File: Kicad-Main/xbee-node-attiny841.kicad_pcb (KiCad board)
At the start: 2 copper layers, 58.5 x 58.5 mm, 41 parts, among them P10 CONN_1, P11 CONN_1, P12 CONN_1, P13 CONN_1, P14 CONN_1, P15 CONN_1, P16 CONN_1, P17 CONN_1, P18 CONN_1, P2 XBee Adaptor, P3 Test, P4 Battery, P5 XBee-ext-1, P6 XBee-ext-2, P7 CONN_1, P8 CONN_1, P9 CONN_1, Q2 S9014, Q3 2N7000, U1 ATTINY84-S, U2 MAX952ESA, U3 TPS77033

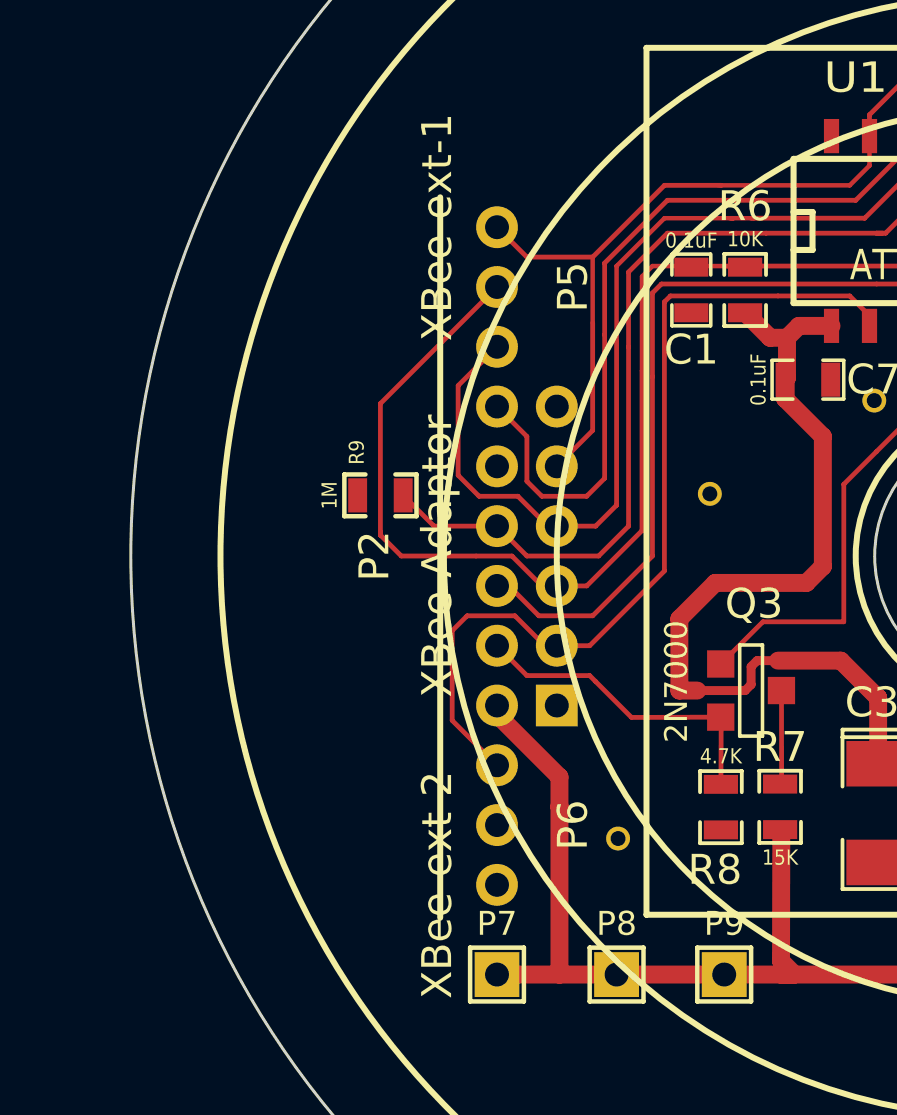
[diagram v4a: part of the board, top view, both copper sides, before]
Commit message: Create version 4 of the XBee mount board and modify the main board to allow the XBee base to sit on the main board.
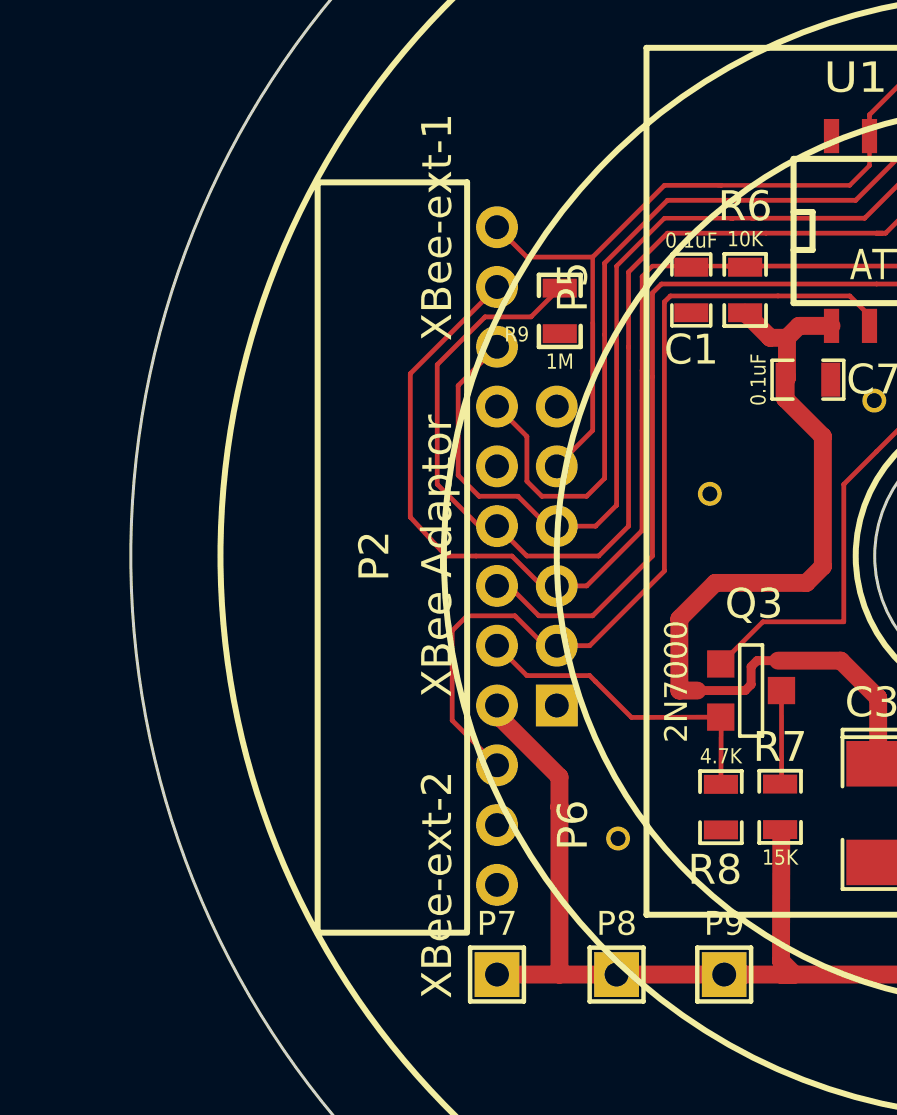
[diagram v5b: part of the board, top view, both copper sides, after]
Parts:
- moved R9 8.61 mm to (185.1, 91.8), turned to 90 degrees
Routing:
- net /Sleep-Rq: track 31.4 -> 39.5 mm
- net /Reset: track 73.8 -> 72.0 mm
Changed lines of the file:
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@@
     (area 162.31 68.7 242.200001 132.330001)
     (thickness 1.6)
-    (drawings 11)
-    (tracks 331)
+    (drawings 14)
+    (tracks 334)
     (zones 0)
     (modules 41)
@@
   )
   (layers
-    (0 F.Cu signal hide)
-    (31 B.Cu power)
+    (0 F.Cu signal)
+    (31 B.Cu power hide)
     (32 B.Adhes user hide)
     (33 F.Adhes user hide)
@@
   )
   (setup
-    (last_trace_width 0.6)
+    (last_trace_width 0.16)
     (user_trace_width 0.3)
     (user_trace_width 0.6)
@@
   )
   (module SMD_Packages:SMD-0603_r (layer F.Cu)
-    (at 179.1 97.97)
-    (attr smd)
-    (fp_text reference R9 (at -0.79 -1.44 90) (layer F.SilkS)
+    (at 185.1 91.8 90)
+    (attr smd)
+    (fp_text reference R9 (at -0.79 -1.44 180) (layer F.SilkS)
       (effects (font (size 0.50038 0.4572) (thickness 0.1143)))
     )
-    (fp_text value 1M (at -1.69926 0 90) (layer F.SilkS)
+    (fp_text value 1M (at -1.69926 0 180) (layer F.SilkS)
       (effects (font (size 0.508 0.4572) (thickness 0.1143)))
     )
@@
     (fp_line (start 1.2065 -0.6985) (end 1.2065 0.6985) (layer F.SilkS) (width 0.15))
     (fp_line (start 1.2065 0.6985) (end 0.50038 0.6985) (layer F.SilkS) (width 0.15))
-    (pad 1 smd rect (at -0.762 0) (size 0.635 1.143) (layers F.Cu F.Paste F.Mask)
-      (net 9 GND))
-    (pad 2 smd rect (at 0.762 0) (size 0.635 1.143) (layers F.Cu F.Paste F.Mask)
+    (pad 1 smd rect (at -0.762 0 90) (size 0.635 1.143) (layers F.Cu F.Paste F.Mask)
+      (net 9 GND))
+    (pad 2 smd rect (at 0.762 0 90) (size 0.635 1.143) (layers F.Cu F.Paste F.Mask)
       (net 5 /Sleep-Rq))
     (model smd\resistors\R0603.wrl
@@
     )
   )
+  (gr_line (start 182 112.6) (end 177 112.6) (angle 90) (layer F.SilkS) (width 0.2))
+  (gr_line (start 182 87.5) (end 177 87.5) (angle 90) (layer F.SilkS) (width 0.2))
+  (gr_line (start 177 112.5) (end 177 87.5) (angle 90) (layer F.SilkS) (width 0.2))
   (gr_circle (center 200 100) (end 215 99.9) (layer F.SilkS) (width 0.2))
   (gr_circle (center 200 100) (end 226.25 100) (layer F.SilkS) (width 0.2))
@@
   (gr_circle (center 200 100) (end 205 100) (layer F.SilkS) (width 0.2))
   (gr_circle (center 200 100) (end 218.75 99) (layer F.SilkS) (width 0.2))
-  (gr_line (start 181.1 112.1) (end 181.1 88) (angle 90) (layer F.SilkS) (width 0.2))
+  (gr_line (start 182 112.5) (end 182 87.5) (angle 90) (layer F.SilkS) (width 0.2))
   (gr_line (start 188 83) (end 188 112) (angle 90) (layer F.SilkS) (width 0.2))
   (gr_line (start 212 83) (end 188 83) (angle 90) (layer F.SilkS) (width 0.2))
@@
   (segment (start 188.6 87.6) (end 186.2 90) (width 0.16) (layer F.Cu) (net 2))
   (segment (start 190.5 87.6) (end 188.6 87.6) (width 0.16) (layer F.Cu) (net 2))
-  (segment (start 182.3 100) (end 179.8 100) (width 0.16) (layer F.Cu) (net 3))
+  (segment (start 182.3 100) (end 181.3 100) (width 0.16) (layer F.Cu) (net 3))
   (segment (start 183.5 100) (end 182.3 100) (width 0.16) (layer F.Cu) (net 3))
   (segment (start 184.5 101) (end 183.5 100) (width 0.16) (layer F.Cu) (net 3))
-  (segment (start 179.8 100) (end 179.1 99.3) (width 0.16) (layer F.Cu) (net 3))
+  (segment (start 181.3 100) (end 180.1 98.7) (width 0.16) (layer F.Cu) (net 3))
   (segment (start 185 101) (end 184.5 101) (width 0.16) (layer F.Cu) (net 3))
-  (segment (start 179.1 94.9) (end 183 91) (width 0.16) (layer F.Cu) (net 3))
-  (segment (start 179.1 99.3) (end 179.1 94.9) (width 0.16) (layer F.Cu) (net 3))
-  (segment (start 179.1 99.2) (end 179.1 99.3) (width 0.16) (layer F.Cu) (net 3))
+  (segment (start 180.1 93.9) (end 183 91) (width 0.16) (layer F.Cu) (net 3))
+  (segment (start 180.1 98.7) (end 180.1 93.9) (width 0.16) (layer F.Cu) (net 3))
   (segment (start 187.85 93.8) (end 187.85 99.15) (width 0.16) (layer F.Cu) (net 3))
   (segment (start 190.7 90.3) (end 188.2 90.3) (width 0.15) (layer F.Cu) (net 3))
@@
   (segment (start 195.3 88.7) (end 191.6 88.7) (width 0.16) (layer F.Cu) (net 4))
   (segment (start 191.6 88.7) (end 191.5 88.7) (width 0.15) (layer F.Cu) (net 4))
-  (segment (start 183 99) (end 180.892 99) (width 0.16) (layer F.Cu) (net 5))
-  (segment (start 180.892 99) (end 179.862 97.97) (width 0.16) (layer F.Cu) (net 5))
+  (segment (start 183 99) (end 182.4 99) (width 0.16) (layer F.Cu) (net 5))
+  (segment (start 182.4 99) (end 181 97.6) (width 0.16) (layer F.Cu) (net 5))
+  (segment (start 184.138 92) (end 185.1 91.038) (width 0.16) (layer F.Cu) (net 5))
+  (segment (start 182.6 92) (end 184.138 92) (width 0.16) (layer F.Cu) (net 5))
+  (segment (start 181 93.6) (end 182.6 92) (width 0.16) (layer F.Cu) (net 5))
+  (segment (start 181 97.6) (end 181 93.6) (width 0.16) (layer F.Cu) (net 5))
   (segment (start 187.4 93) (end 187.4 99) (width 0.16) (layer F.Cu) (net 5))
   (segment (start 191 89.2) (end 188.7 89.2) (width 0.16) (layer F.Cu) (net 5))

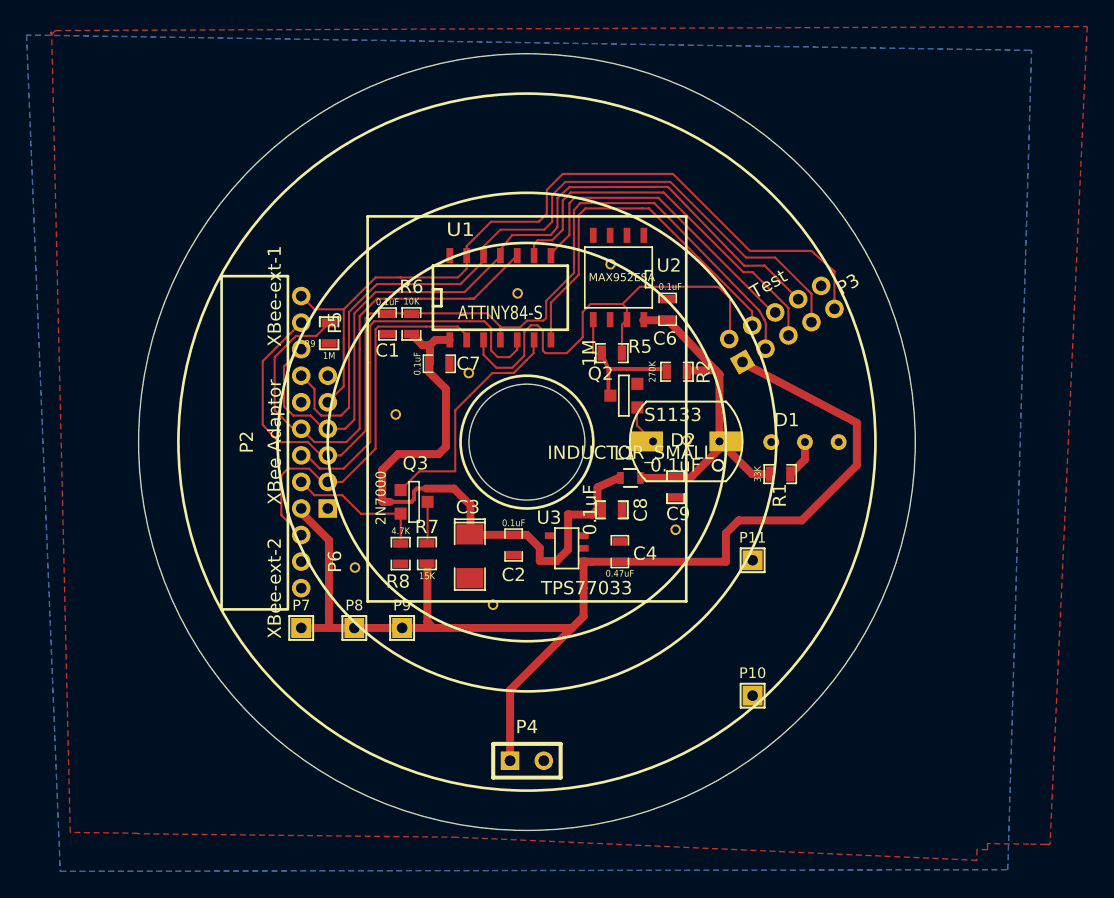
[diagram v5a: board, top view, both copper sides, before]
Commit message: Major new version of the PCBs for next stage of production run.
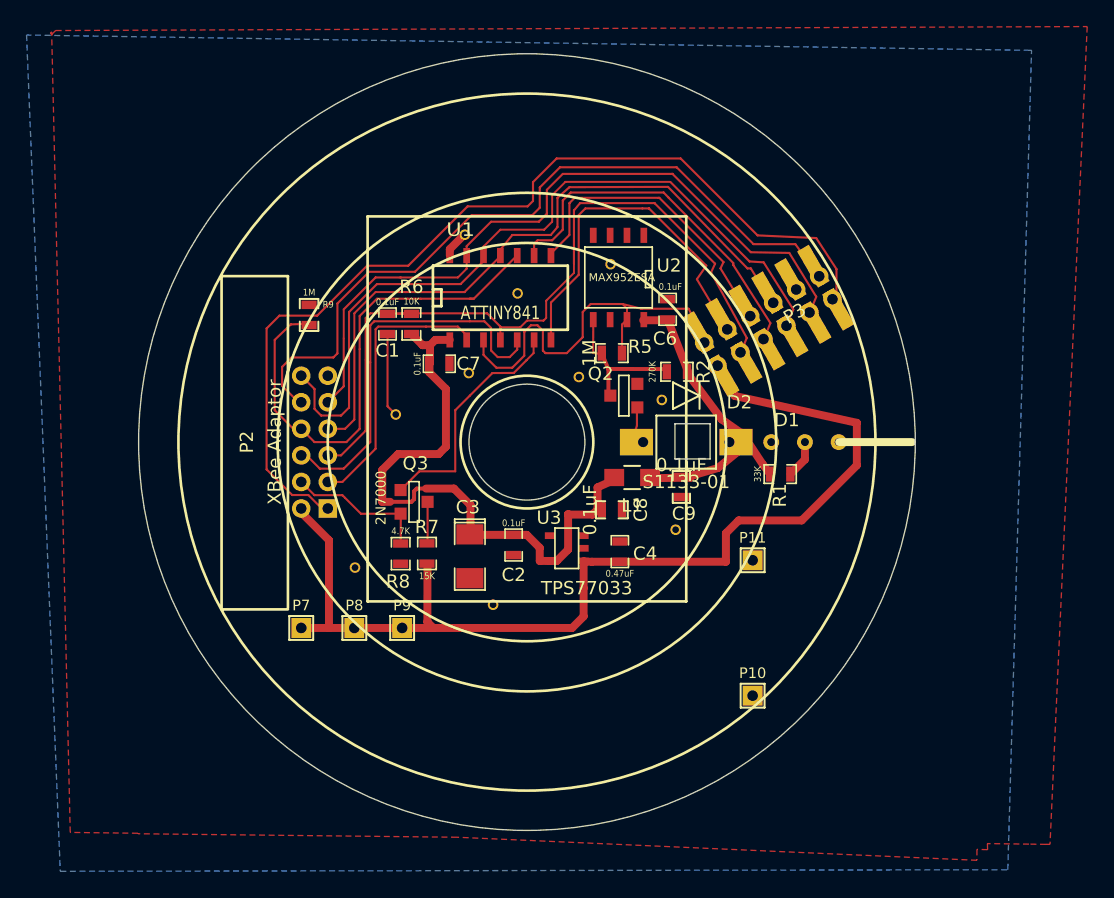
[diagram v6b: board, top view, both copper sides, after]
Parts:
- removed P4: Battery, Connect:SIL-2
- removed P5: XBee-ext-1, Photodiode:pin_header_2mm_1x3
- removed P6: XBee-ext-2, Photodiode:pin_header_2mm_1x3
- added P19: CONN_1, PhotoDiode:THROUGHVIA, F.Cu at (195.3, 84.4)
- added P20: CONN_1, PhotoDiode:THROUGHVIA, F.Cu at (203.9, 95.1)
- D2: value S1133 -> S1133-01; footprint Photodiode:S1133TH -> PhotoDiode:BPW34
- L1: footprint Resistors_SMD:R_0603 -> PhotoDiode:R_0805
- P3: value Test -> Debug Adaptor; footprint PhotoDiode:pin_header_2mm_2x5 -> PhotoDiode:pin_smd_header_2mm_2x6
- U1: value ATTINY84-S -> ATTINY841
- moved P14 3.57 mm to (210.2, 96.8)
- moved R9 2.04 mm to (183.6, 90.4), turned to 270 degrees
- moved P3 0.74 mm to (219.0, 90.4)
- moved C9 0.43 mm to (211.6, 103.4)
- moved L1 0.13 mm to (207.9, 102.7)
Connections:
- P2 pad 1: Net-(P2-Pad1) -> /Commissioning
- P2 pad 10: Net-(P2-Pad10) -> /Association
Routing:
- net /Commissioning: track 0.00 -> 71.6 mm
- net /Association: track 0.00 -> 56.8 mm
- net /Reset: track 72.0 -> 59.3 mm
- net /Rx: track 61.9 -> 52.0 mm
- net /Bootloader: track 30.4 -> 21.6 mm
- net GND: track 0.04 -> 8.43 mm
- net VDD: track 46.9 -> 53.9 mm
- net /Battery: track 91.1 -> 84.3 mm
- net /On/Sleep: track 60.3 -> 55.2 mm
- net /Count: track 34.6 -> 30.8 mm
- net /VDDA: track 27.1 -> 24.9 mm
- net /Tx: track 59.5 -> 58.4 mm
- net /MISO: track 24.1 -> 23.1 mm
- net /SCK: track 28.6 -> 27.7 mm
- net /Sleep-Rq: track 39.5 -> 38.8 mm
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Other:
- outline, holes or cut-outs redrawn

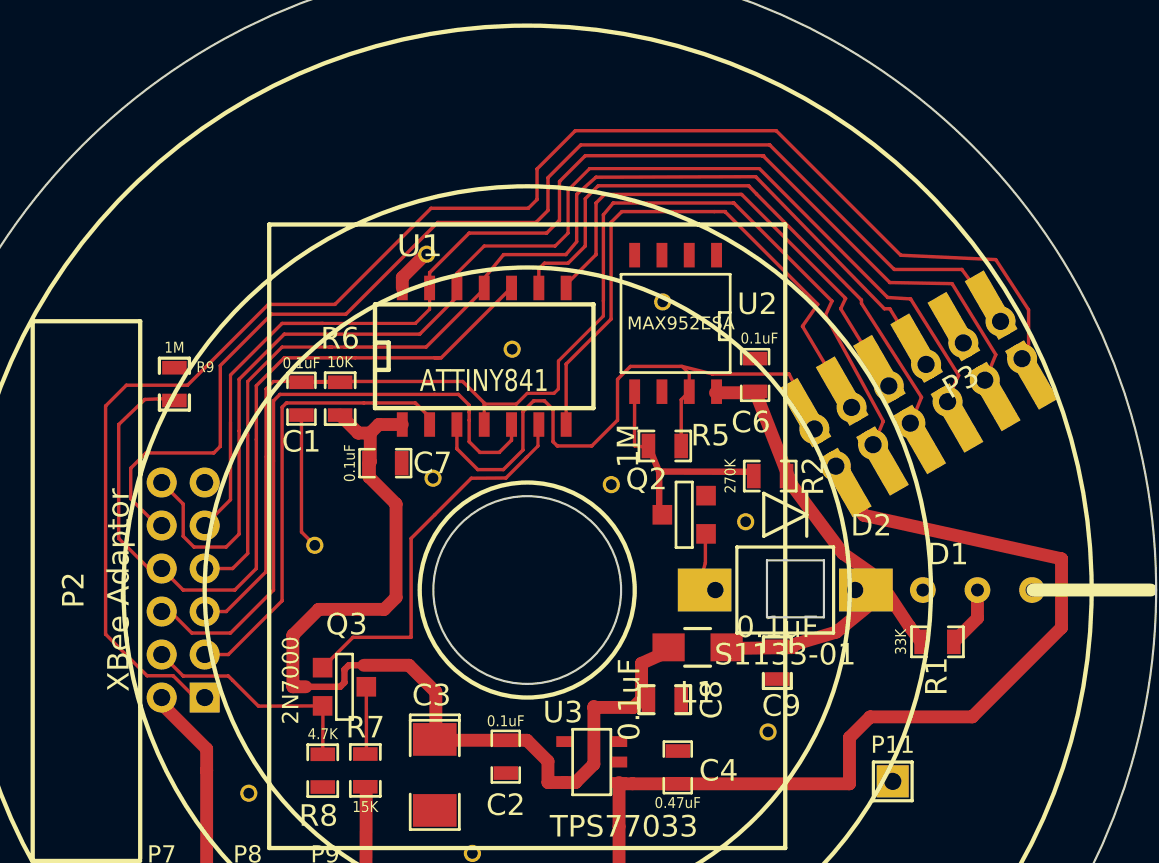
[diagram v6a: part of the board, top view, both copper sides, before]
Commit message: Main PCB. Changes to debug connector to bring out XBee association and commissioning signals. Change photodiode to BPW34. Minor change to battery mount to increase drill hole and move holes to spec. The LED mount footprint has also been changed to match the power and ground on the mounting board itself.
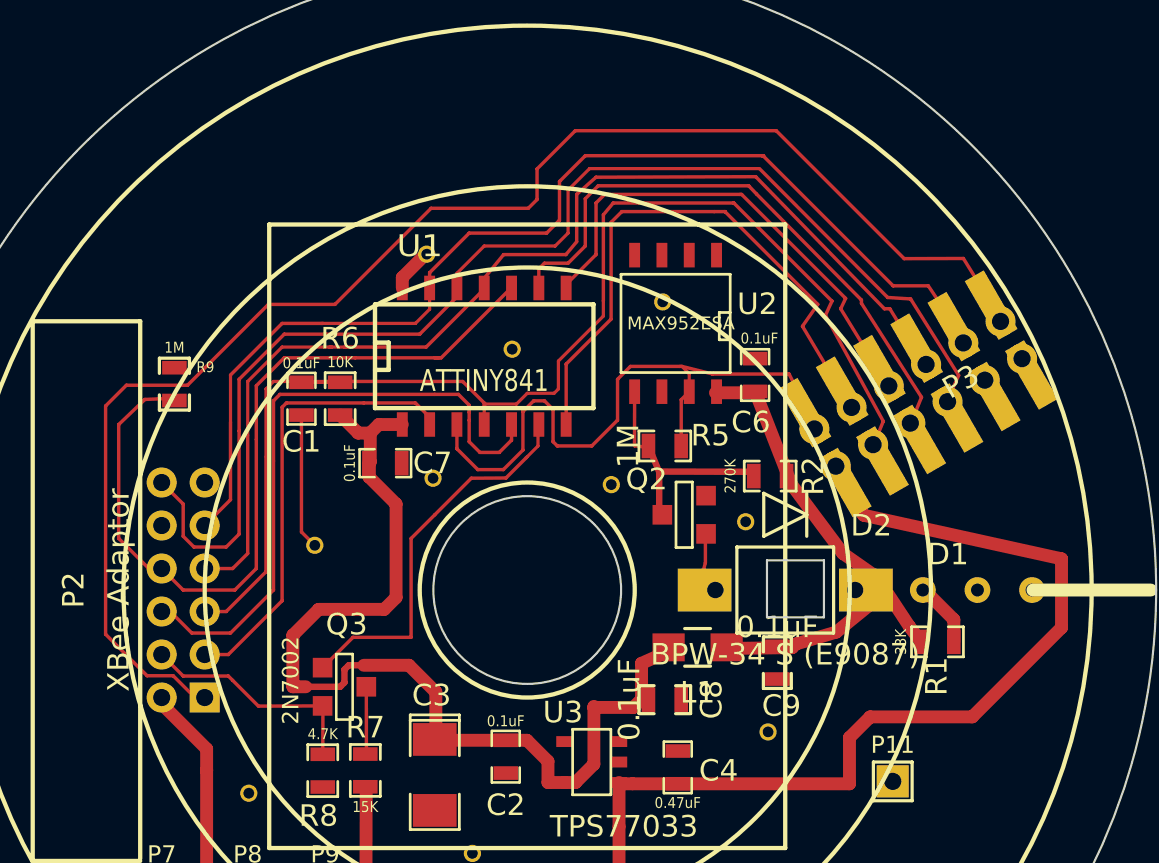
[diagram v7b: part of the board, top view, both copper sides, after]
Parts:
- D2: value S1133-01 -> BPW-34 S (E9087)
- Q2: value S9014 -> MMBT3904
- Q3: value 2N7000 -> 2N7002
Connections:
- P3 pad 10: GND -> /On/Sleep
- P3 pad 11: /Commissioning -> GND
- P3 pad 12: /Association -> /Commissioning
- P3 pad 9: /On/Sleep -> /Association
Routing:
- net /Association: track 56.8 -> 0.20 mm
- net /Commissioning: track 71.6 -> 66.7 mm
- net /On/Sleep: track 55.2 -> 51.9 mm
